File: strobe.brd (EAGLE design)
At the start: 160 x 100 mm, 38 parts, among them IC1 AT90USB162A, Q1 IRF3704S, Q2 IRF3704S, T5 BC849, T6 BC849

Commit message: Poprawki Schematów
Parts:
- C4, C5: device rcl:C0805 -> rcl:C0603
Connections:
- net GND: now also C1.2, C4.2, C5.2
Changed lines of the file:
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@@
 <attribute name="OC_FARNELL" value="unknown" x="57.15" y="6.35" size="1.778" layer="27" display="off"/>
 </element>
-<element name="C4" library="rcl" package="C0805" value="22Pf" x="25.4" y="41.91"/>
-<element name="C5" library="rcl" package="C0805" value="22Pf" x="33.02" y="41.91" rot="R180"/>
+<element name="C4" library="rcl" package="C0603" value="22Pf" x="25.4" y="41.91"/>
+<element name="C5" library="rcl" package="C0603" value="22Pf" x="33.02" y="41.91" rot="R180"/>
 <element name="R8" library="rcl" package="R0805" value="10K" x="33.02" y="58.42" rot="R90"/>
 <element name="IC2" library="SparkFun-PowerIC" package="SOT223" value="" x="38.1" y="57.15"/>
@@
 <wire x1="22.3774" y1="56.28" x2="19.459196875" y2="56.28" width="0.4064" layer="1"/>
 <wire x1="19.459196875" y1="56.28" x2="19.040684375" y2="56.6985125" width="0.4064" layer="1"/>
+<contactref element="C5" pad="2"/>
+<contactref element="C4" pad="2"/>
+<contactref element="C1" pad="2"/>
 </signal>
 <signal name="N$3">
@@
 <wire x1="24.67" y1="47.72" x2="24.67" y2="51.5874" width="0.3048" layer="1"/>
 <wire x1="34.036" y1="45.72" x2="33.97" y2="45.654" width="0.3048" layer="1"/>
-<wire x1="33.97" y1="45.654" x2="33.97" y2="41.91" width="0.3048" layer="1"/>
+<wire x1="33.97" y1="45.654" x2="33.87" y2="41.91" width="0.3048" layer="1"/>
 </signal>
 <signal name="N$13">
@@
 <wire x1="23.87" y1="46.234" x2="23.87" y2="51.5874" width="0.3048" layer="1"/>
 <wire x1="24.384" y1="45.72" x2="24.45" y2="45.654" width="0.3048" layer="1"/>
-<wire x1="24.45" y1="45.654" x2="24.45" y2="41.91" width="0.3048" layer="1"/>
+<wire x1="24.45" y1="45.654" x2="24.55" y2="41.91" width="0.3048" layer="1"/>
 </signal>
 <signal name="N$14">

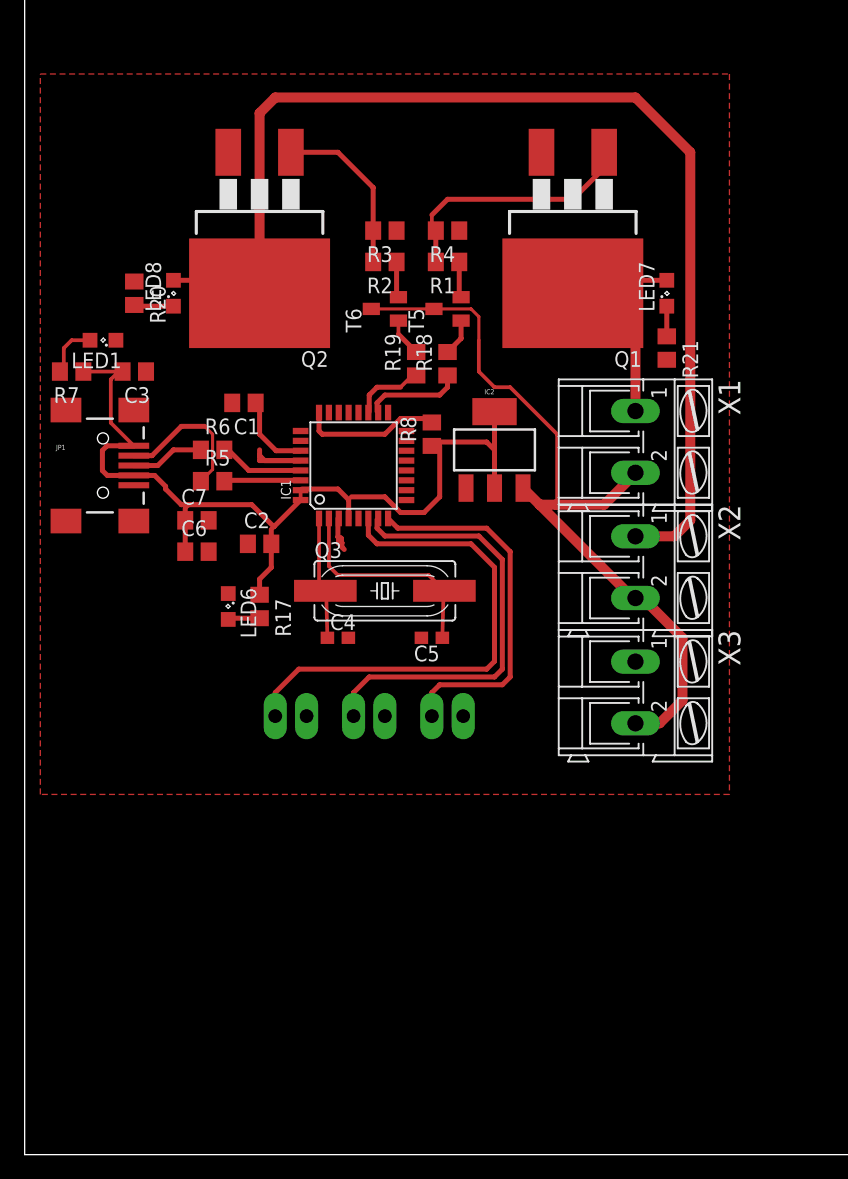
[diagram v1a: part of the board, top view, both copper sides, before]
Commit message: Nowa płytka
4 lampy + RJ45
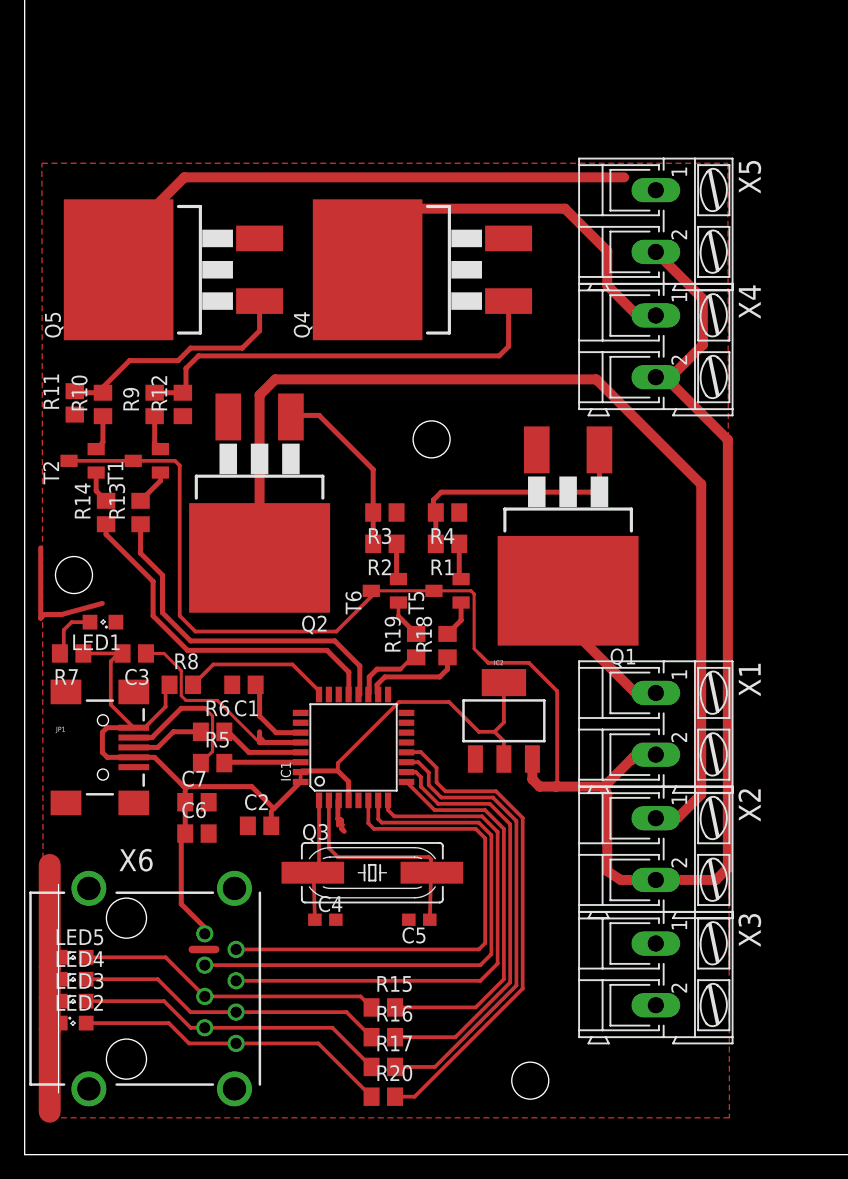
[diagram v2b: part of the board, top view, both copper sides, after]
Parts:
- removed JP4, JP5, JP7: (no value), SparkFun-Connectors:1X02_LONGPADS
- removed LED6, LED7, LED8: (no value), led:SML0805
- removed R21: (no value), rcl:R0805
- added LED2, LED3, LED4, LED5: (no value), led:SML0805
- added Q4, Q5: IRF3704S, transistor-power:D2PACK
- added R10, R11, R12, R13, R14, R15, R16, R9: (no value), rcl:R0805
- added T1, T2: BC849, transistor:SOT23
- added X4, X5: (no value), con-ptr500:AK300/2
- added X6: RJ45-6LC21-B, con-tycoelectronics:RJ45-SHIELD1
- R17: value 340 -> (none)
- moved R20 68.2 mm to (29.1, 4.70), turned to 0 degrees
- moved R17 38.7 mm to (29.1, 7.11), turned to 0 degrees
- moved R8 28.7 mm to (12.7, 38.1), turned to 0 degrees
- moved Q1 24.1 mm to (44.1, 48.3)
- moved X3 22.9 mm to (51.2, 14.6)
- moved X1 22.9 mm to (51.2, 34.9)
- moved X2 22.9 mm to (51.2, 24.8)
- moved Q3 22.9 mm to (28.2, 22.9)
- moved C4 22.9 mm to (24.4, 19.1)
- moved C5 22.9 mm to (32.0, 19.1)
- moved LED1 22.9 mm to (6.35, 43.2)
- moved R18 22.9 mm to (34.3, 41.3)
- moved R19 22.9 mm to (31.8, 41.3)
- moved R3 22.9 mm to (29.2, 52.1)
- moved R4 22.9 mm to (34.3, 52.1)
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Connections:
- removed net N$27: LED6.A, R17.2
- removed net N$32: LED8.C, R20.2
- removed net N$33: LED7.C, R21.1
- new net CH3: IC1.20, R13.1
- new net CH4: IC1.21, R14.1
- new net L1: LED2.A, R20.1, X6.8
- new net L2: LED3.A, R17.1, X6.7
- new net L3: LED4.A, R16.1, X6.6
- new net L4: LED5.A, R15.1, X6.5
- new net N$11: Q4.1, R12.2, R9.2
- new net N$15: Q5.1, R10.2, R11.2
- new net N$16: Q4.2, X4.1
- new net N$17: Q5.2, X5.1
- new net N$18: R9.1, T1.2
- new net N$19: R10.1, T2.2
- new net N$20: R13.2, T1.1
- new net N$21: R14.2, T2.1
- new net O3: IC1.10, R16.2
- new net O4: IC1.9, R15.2
- net 12V: now also T1.3, T2.3, X4.2, X5.2
- net 5V: now also X6.1; no longer R17.1
- net B1: now also X6.2; no longer JP4.1
- net B2: now also X6.3; no longer JP5.1
- net B3: now also X6.4; no longer JP7.1
- net GND: now also LED2.C, LED3.C, LED4.C, LED5.C, Q4.3, Q5.3, R11.1, R12.1, X6.S1, X6.S2, X6.S3, X6.S4; no longer JP4.2, JP5.2, JP7.2, LED6.C, R20.1, R21.2
- net N$3: no longer LED7.A
- net N$4: no longer LED8.A
- net O1: now also IC1.12, R20.2; no longer IC1.21
- net O2: now also IC1.11, R17.2; no longer IC1.20
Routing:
- net 12V: track 64.1 -> 158.8 mm
- net GND: track 13.3 -> 67.3 mm
- net N$17: track 0.00 -> 45.4 mm
- net O1: track 0.00 -> 40.2 mm
- net O2: track 0.00 -> 37.4 mm
- net N$11: track 0.00 -> 35.3 mm
- net O3: track 0.00 -> 34.6 mm
- net O4: track 0.00 -> 31.4 mm
- net N$16: track 0.00 -> 31.4 mm
- net CH4: track 0.00 -> 28.6 mm
- net CH3: track 0.00 -> 28.1 mm
- net L1: track 0.00 -> 25.6 mm
- net L2: track 0.00 -> 25.4 mm
- net L3: track 0.00 -> 25.1 mm
- net L4: track 0.00 -> 24.8 mm
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
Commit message: board fix
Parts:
- added C8, C9: 100N, rcl:C0805
- added D1: (no value), diode:SMB
- added LED6: (no value), led:SML0805
- added R21: 340, rcl:R0805
- added R22, R24, R26, R28: (no value), rcl:R0805
- added T3, T4, T7, T8: BC849, transistor:SOT23
- added TP1, TP2, TP3, TP4: TPB1,27, testpad:B1,27
- moved R16 4.10 mm to (25.1, 10.4)
- moved R15 4.06 mm to (25.1, 12.6)
- moved R17 4.00 mm to (25.1, 6.91)
- moved R20 4.00 mm to (25.1, 4.70)
- moved R18 0.70 mm to (34.3, 42.0)
- moved R19 0.70 mm to (31.8, 42.0)
- moved IC2 0.60 mm to (38.9, 35.8)
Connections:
- new net N$22: IC1.17, TP1.TP
- new net N$23: LED6.A, R21.2
- new net N$24: R22.2, T3.1
- new net N$25: IC1.16, TP2.TP
- new net N$27: R24.2, T4.1
- new net N$32: IC1.15, TP3.TP
- new net N$34: R26.2, T7.1
- new net N$37: R28.2, T8.1
- new net T1: IC1.12, R22.1
- new net T2: IC1.11, R24.1
- new net T3: IC1.10, R26.1
- new net T4: IC1.9, R28.1
- net 12V: now also C8.1, D1.C, R21.1
- net 5V: now also C9.1, D1.A, T3.3, T4.3, T7.3, T8.3
- net GND: now also C8.2, C9.2, LED6.C
- net N$14: now also TP4.TP
- net O1: now also T3.2; no longer IC1.12
- net O2: now also T4.2; no longer IC1.11
- net O3: now also T7.2; no longer IC1.10
- net O4: now also T8.2; no longer IC1.9
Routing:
- net 5V: track 83.2 -> 161.2 mm
- net T1: track 0.00 -> 35.7 mm
- net O1: track 40.2 -> 4.82 mm
- net T2: track 0.00 -> 32.0 mm
- net O3: track 34.6 -> 3.31 mm
- net O2: track 37.4 -> 8.30 mm
- net T3: track 0.00 -> 28.2 mm
- net 12V: track 158.8 -> 185.9 mm
- net O4: track 31.4 -> 7.77 mm
- net T4: track 0.00 -> 23.3 mm
- net N$24: track 0.00 -> 7.64 mm
- net N$34: track 0.00 -> 7.63 mm
- net L3: track 25.1 -> 20.7 mm
- net L4: track 24.8 -> 20.6 mm
- net L2: track 25.4 -> 21.5 mm
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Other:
- board text added: "STROBE"
- board text added: "inventorsgroup.pl"

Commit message: PCB extreme makeover
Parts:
- removed D1: (no value), diode:SMB
- removed LED2, LED3, LED4, LED5: (no value), led:SML0805
- removed X6: RJ45-6LC21-B, con-tycoelectronics:RJ45-SHIELD1
- added R23, R25, R27: (no value), rcl:R0805
- added T9: BC849, transistor:SOT23
- added U$1: RJ45, RJ45:RJ45
- JP1: value USBSMD -> USB-B; device SparkFun-Connectors:USB-MINIB -> SparkFun-Connectors:USB-B-PTH
- moved C7 17.7 mm to (17.4, 46.0), turned to 90 degrees
- moved R8 10.7 mm to (19.9, 46.0), turned to 90 degrees
- moved TP4 9.62 mm to (22.7, 46.9)
- moved C4 8.26 mm to (25.4, 27.2)
- moved C5 8.26 mm to (33.0, 27.2)
- moved R20 8.25 mm to (26.0, 12.9), turned to 180 degrees
- moved R17 8.24 mm to (26.0, 15.1), turned to 180 degrees
- moved R16 8.13 mm to (26.0, 18.5), turned to 180 degrees
- moved R15 8.11 mm to (26.0, 20.7), turned to 180 degrees
- moved C6 8.07 mm to (15.0, 34.0), turned to 270 degrees
- moved Q4 8.06 mm to (31.4, 79.8)
- moved Q5 8.06 mm to (11.2, 79.8)
- moved X5 8.06 mm to (52.2, 83.7)
- moved C9 8.06 mm to (44.2, 47.0)
- moved Q1 8.06 mm to (45.1, 56.3)
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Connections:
- removed net L1: LED2.A, R20.1, X6.8
- removed net L2: LED3.A, R17.1, X6.7
- removed net L3: LED4.A, R16.1, X6.6
- removed net L4: LED5.A, R15.1, X6.5
- new net N$26: R25.1, U$1.L1+
- new net N$33: R15.2, U$1.5
- new net N$35: R16.2, U$1.6
- new net N$36: R17.2, U$1.7
- new net N$38: R20.2, U$1.8
- new net N$39: R23.2, T9.1
- new net N$40: R27.1, U$1.L2+
- new net O5: R25.2, T9.2
- new net T5: IC1.5, R23.1
- net 12V: no longer D1.C
- net 5V: now also R27.2, T9.3, U$1.1; no longer D1.A, X6.1
- net B1: now also U$1.2; no longer X6.2
- net B2: now also U$1.3; no longer X6.3
- net B3: now also U$1.4; no longer X6.4
- net GND: now also U$1.L1-, U$1.L2-; no longer LED2.C, LED3.C, LED4.C, LED5.C, X6.S1, X6.S2, X6.S3, X6.S4
- net O1: now also R20.1; no longer R20.2
- net O2: now also R17.1; no longer R17.2
- net O3: now also R16.1; no longer R16.2
- net O4: now also R15.1; no longer R15.2
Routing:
- net GND: track 67.3 -> 0.03 mm
- net 5V: track 161.2 -> 209.6 mm
- net T5: track 0.00 -> 37.5 mm
- net N$40: track 0.00 -> 24.1 mm
- net L1: track 22.9 -> 0.00 mm
- net N$38: track 0.00 -> 21.8 mm
- net L2: track 21.5 -> 0.00 mm
- net L3: track 20.7 -> 0.00 mm
- net L4: track 20.6 -> 0.00 mm
- net N$35: track 0.00 -> 19.5 mm
- net N$36: track 0.00 -> 19.3 mm
- net N$33: track 0.00 -> 17.6 mm
- net B1: track 40.8 -> 53.6 mm
- net B3: track 42.9 -> 55.5 mm
- net N$14: track 14.5 -> 5.93 mm
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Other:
- board size 160 x 100 mm -> 63 x 99 mm

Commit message: Close-to-final version of board
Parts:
- removed R23, R25, R27: (no value), rcl:R0805
- removed T9: BC849, transistor:SOT23
- removed X1, X2, X3, X4, X5: (no value), con-ptr500:AK300/2
- added F1: FUSEX20MM, SparkFun-Passives:FUSE_5MM
- added X6: D-SUB9-H3M09RA, con-thomas-betts:H3M09RA
- U$1: value RJ45 -> MF42-10; device RJ45:RJ45 -> con-amphenol:MF42-10
- moved Q5 71.6 mm to (27.9, 10.1), flipped to the bottom, turned to 180 degrees
- moved U$1 64.7 mm to (58.0, 4.83), turned to 90 degrees
- moved R11 53.8 mm to (19.9, 17.2), flipped to the bottom, turned to 270 degrees
- moved R10 53.7 mm to (22.4, 17.3), flipped to the bottom, turned to 270 degrees
- moved Q2 52.9 mm to (40.1, 10.0), flipped to the bottom
- moved Q4 46.8 mm to (27.9, 33.0), flipped to the bottom, turned to 180 degrees
- moved T2 45.7 mm to (21.0, 21.2), flipped to the bottom, turned to 270 degrees
- moved R3 41.7 mm to (35.1, 18.7), flipped to the bottom, turned to 270 degrees
- moved R2 39.8 mm to (40.3, 19.0), flipped to the bottom, turned to 270 degrees
- moved R19 37.6 mm to (48.0, 15.6), flipped to the bottom
- moved R7 37.3 mm to (29.4, 9.64), turned to 180 degrees
- moved T6 36.8 mm to (46.6, 20.8), flipped to the bottom, turned to 0 degrees
- moved LED1 36.4 mm to (25.4, 9.59), turned to 0 degrees
- moved R14 35.7 mm to (19.4, 26.3), flipped to the bottom, turned to 270 degrees
- moved R9 27.2 mm to (26.0, 45.7), flipped to the bottom, turned to 0 degrees
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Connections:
- removed net N$16: Q4.2, X4.1
- removed net N$17: Q5.2, X5.1
- removed net N$38: R20.2, U$1.8
- removed net N$39: R23.2, T9.1
- removed net N$4: Q2.2, X2.1
- removed net N$40: R27.1, U$1.L2+
- removed net O5: R25.2, T9.2
- new net L1: Q1.2, U$1.6
- new net L2: Q2.2, U$1.9
- new net L3: Q4.2, U$1.7
- new net L4: Q5.2, U$1.10
- net 12V: now also F1.1, U$1.2, U$1.3, U$1.4, U$1.5; no longer X1.2, X2.2, X3.2, X4.2, X5.2
- net 5V: now also X6.9; no longer R27.2, T9.3, U$1.1
- net B1: now also X6.4; no longer U$1.2
- net B2: now also X6.8; no longer U$1.3
- net B3: now also X6.3; no longer U$1.4
- net GND: now also U$1.11, U$1.12, U$1.8, X6.5; no longer U$1.L1-, U$1.L2-, X3.1
- net N$26: now also R20.2, X6.1; no longer R25.1, U$1.L1+
- net N$3: now also F1.3, U$1.1; no longer Q1.2, X1.1
- net N$33: now also R17.2, X6.6; no longer R15.2, U$1.5
- net N$35: now also X6.2; no longer U$1.6
- net N$36: now also R15.2, X6.7; no longer R17.2, U$1.7
- net T5: no longer R23.1
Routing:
- net N$4: track 89.2 -> 0.00 mm
- net CH2: track 6.77 -> 69.8 mm, vias 0 -> 1
- net N$17: track 48.4 -> 0.00 mm
- net T5: track 37.5 -> 0.00 mm
- net 12V: track 180.5 -> 216.7 mm, vias 0 -> 2
- net L3: track 0.00 -> 33.8 mm
- net L4: track 0.00 -> 31.4 mm
- net N$16: track 31.4 -> 0.00 mm
- net N$11: track 35.3 -> 6.51 mm
- net N$40: track 24.1 -> 0.00 mm
- net N$38: track 21.8 -> 0.00 mm
- net CH3: track 28.1 -> 9.99 mm, vias 0 -> 1
- net L1: track 0.00 -> 16.8 mm
- net 5V: track 209.6 -> 193.9 mm
- net L2: track 0.00 -> 15.2 mm
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- added copper zone on layer 16, net GND
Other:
- board size 63 x 99 mm -> 73.7 x 71.1 mm
- board text removed: "STROBE"

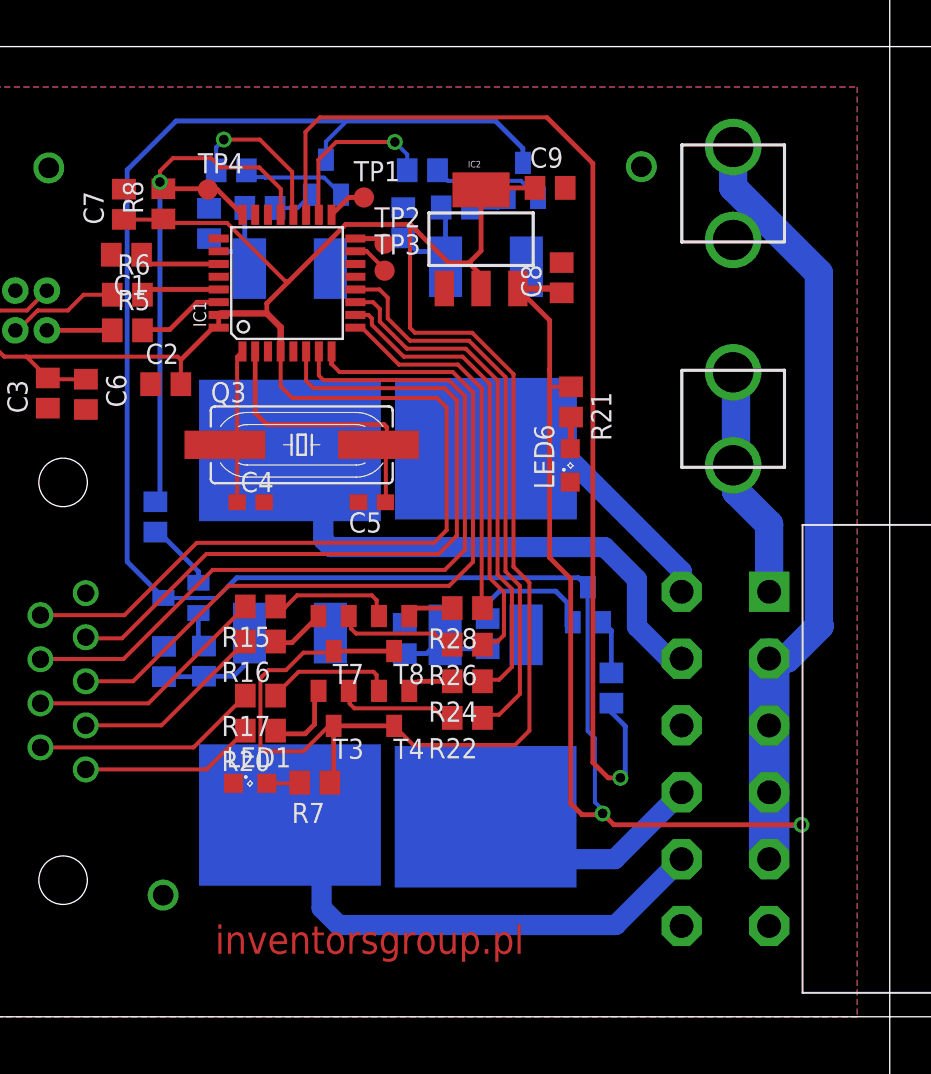
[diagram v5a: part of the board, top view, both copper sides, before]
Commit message: bezpiecznik out
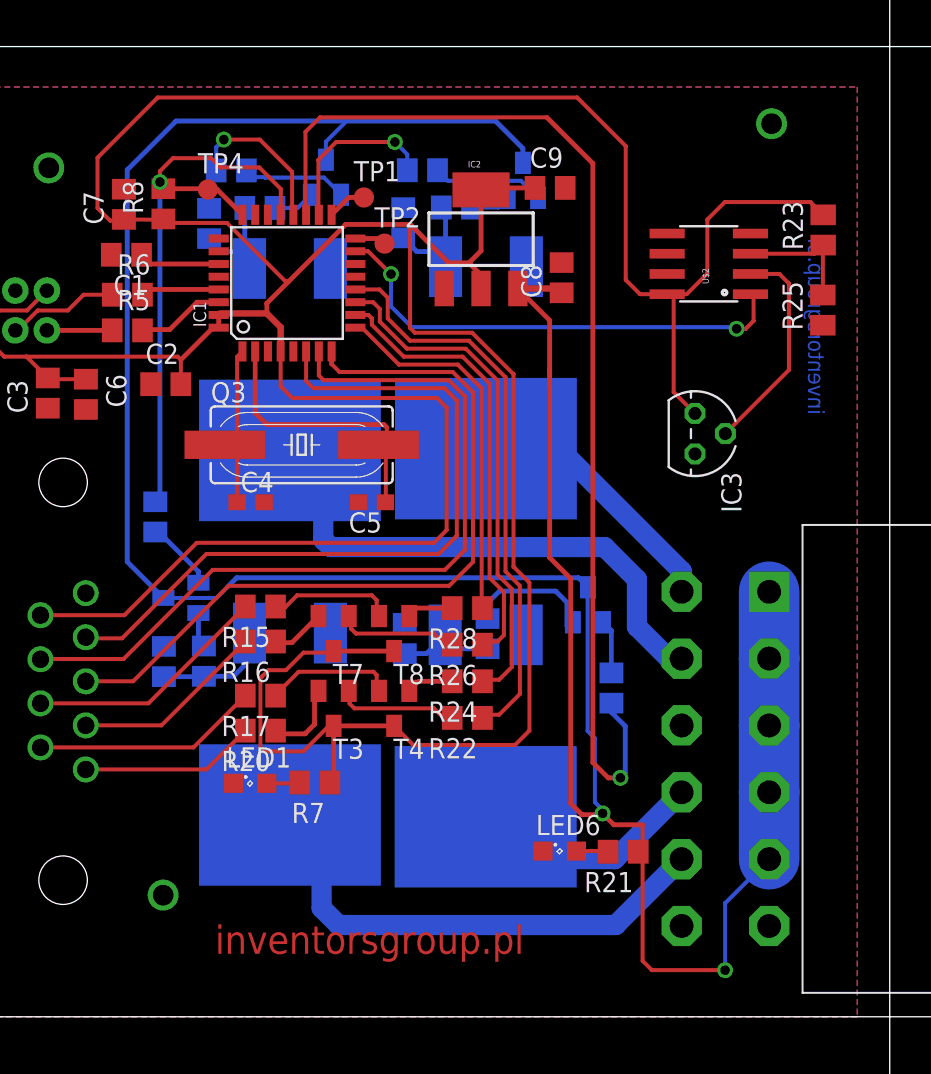
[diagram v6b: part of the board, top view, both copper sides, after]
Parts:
- removed F1: FUSEX20MM, SparkFun-Passives:FUSE_5MM
- removed TP3: TPB1,27, testpad:B1,27
- added IC3: LM35CZ, lm35:TO92
- added R23, R25: (no value), rcl:M0805
- added U$2: LM393, SparkFun-AnalogIC:SO08
- moved R21 28.5 mm to (48.8, 5.29), turned to 180 degrees
- moved LED6 24.2 mm to (44.8, 5.33), turned to 0 degrees
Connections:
- removed net N$32: IC1.15, TP3.TP
- new net N$4: R23.1, R25.2, U$2.3
- new net TEMP: IC1.15, U$2.1
- net 12V: now also U$1.1; no longer F1.1
- net 5V: now also IC3.1, R23.2, U$2.8
- net GND: now also IC3.3, R25.1, U$2.4
- net N$3: now also IC3.2, U$2.2; no longer F1.3, U$1.1
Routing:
- net 5V: track 193.9 -> 270.0 mm
- net TEMP: track 0.00 -> 30.2 mm, vias 0 -> 2
- net 12V: track 216.7 -> 193.0 mm
- net N$4: track 0.00 -> 7.94 mm
- net N$32: track 2.40 -> 0.00 mm
- net N$3: track 15.0 -> 13.8 mm
